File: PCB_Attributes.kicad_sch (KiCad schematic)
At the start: 0 parts

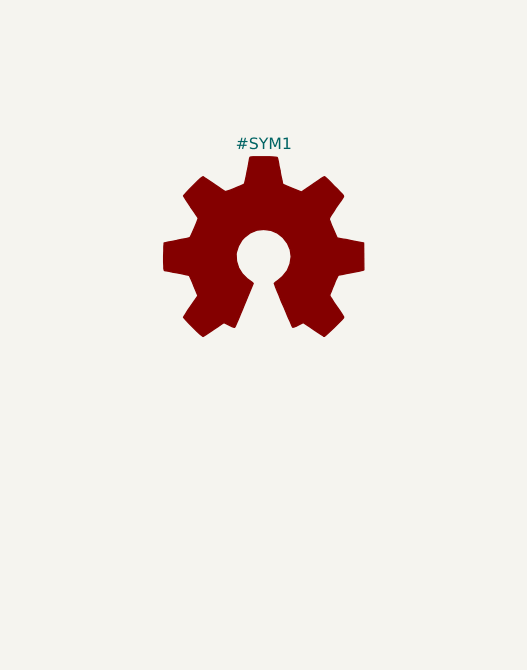
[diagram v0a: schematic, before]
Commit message: Changed GPIO headers to Arduino style
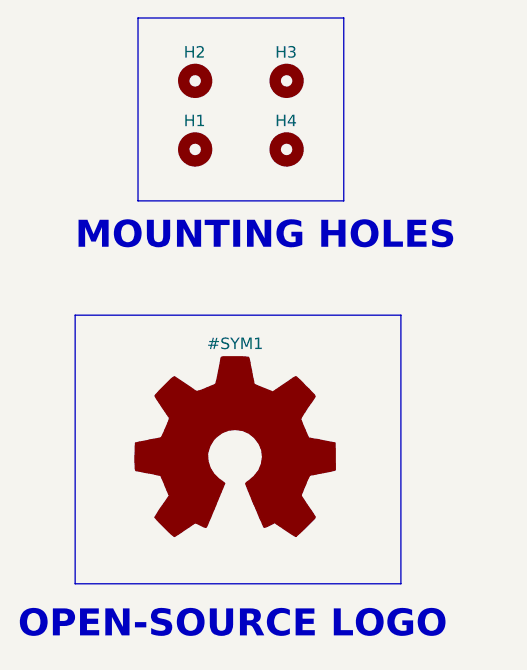
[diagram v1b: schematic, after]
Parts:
- added H1, H2, H3, H4: MountingHole, symbol ESP32-S3_DB:MountingHole
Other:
- note added: "MOUNTING HOLES"
- note added: "OPEN-SOURCE LOGO"
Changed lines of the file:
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@@
 (kicad_sch (version 20230121) (generator eeschema)
   (paper "A4")
-  (symbol (lib_id "ESP32-S3_DB:Logo_Open_Hardware_Large") (at 151.13 99.695 0) (unit 1)
+  (bus (pts (xy 130.175 106.045) (xy 166.37 106.045))
+    (stroke (width 1) (type default) (color 72 72 72 1))
+  )
+  (bus (pts (xy 130.175 135.89) (xy 130.175 106.045))
+    (stroke (width 1) (type default) (color 72 72 72 1))
+  )
+  (bus (pts (xy 166.37 106.045) (xy 166.37 135.89))
+    (stroke (width 1) (type default) (color 72 72 72 1))
+  )
+  (bus (pts (xy 130.175 135.89) (xy 166.37 135.89))
+    (stroke (width 1) (type default) (color 72 72 72 1))
+  )
+  (bus (pts (xy 137.16 93.345) (xy 137.16 73.025))
+    (stroke (width 1) (type default) (color 72 72 72 1))
+  )
+  (bus (pts (xy 137.16 93.345) (xy 160.02 93.345))
+    (stroke (width 1) (type default) (color 72 72 72 1))
+  )
+  (bus (pts (xy 137.16 73.025) (xy 160.02 73.025))
+    (stroke (width 1) (type default) (color 72 72 72 1))
+  )
+  (bus (pts (xy 160.02 73.025) (xy 160.02 93.345))
+    (stroke (width 1) (type default) (color 72 72 72 1))
+  )
+  (text "OPEN-SOURCE LOGO" (at 123.825 142.24 0)
+    (effects (font (size 3 3) bold (color 255 0 0 1)) (justify left bottom))
+  )
+  (text "MOUNTING HOLES" (at 130.175 99.06 0)
+    (effects (font (size 3 3) bold (color 255 0 0 1)) (justify left bottom))
+  )
+  (symbol (lib_id "ESP32-S3_DB:MountingHole") (at 143.51 87.63 0) (unit 1)
+    (in_bom yes) (on_board yes) (dnp no)
+    (property "Reference" "H1" (at 142.24 84.455 0)
+      (effects (font (size 1.27 1.27)) (justify left))
+    )
+    (property "Value" "MountingHole" (at 146.05 88.9 0)
+      (effects (font (size 1.27 1.27)) (justify left) hide)
+    )
+    (property "Footprint" "" (at 143.51 87.63 0)
+      (effects (font (size 1.27 1.27)) hide)
+    )
+    (property "Datasheet" "~" (at 143.51 87.63 0)
+      (effects (font (size 1.27 1.27)) hide)
+    )
+    (instances
+      (project "ESP32-S3_DB"
+        (path "/b7fc4bd3-c219-4455-832b-8d795385dcf1/7ada9602-7e0d-4ea4-a634-9a5d8155ae8b"
+          (reference "H1") (unit 1)
+        )
+      )
+    )
+  )
+  (symbol (lib_id "ESP32-S3_DB:MountingHole") (at 153.67 80.01 0) (unit 1)
+    (in_bom yes) (on_board yes) (dnp no)
+    (property "Reference" "H3" (at 152.4 76.835 0)
+      (effects (font (size 1.27 1.27)) (justify left))
+    )
+    (property "Value" "MountingHole" (at 156.21 81.28 0)
+      (effects (font (size 1.27 1.27)) (justify left) hide)
+    )
+    (property "Footprint" "" (at 153.67 80.01 0)
+      (effects (font (size 1.27 1.27)) hide)
+    )
+    (property "Datasheet" "~" (at 153.67 80.01 0)
+      (effects (font (size 1.27 1.27)) hide)
+    )
+    (instances
+      (project "ESP32-S3_DB"
+        (path "/b7fc4bd3-c219-4455-832b-8d795385dcf1/7ada9602-7e0d-4ea4-a634-9a5d8155ae8b"
+          (reference "H3") (unit 1)
+        )
+      )
+    )
+  )
+  (symbol (lib_id "ESP32-S3_DB:MountingHole") (at 153.67 87.63 0) (unit 1)
+    (in_bom yes) (on_board yes) (dnp no)
+    (property "Reference" "H4" (at 152.4 84.455 0)
+      (effects (font (size 1.27 1.27)) (justify left))
+    )
+    (property "Value" "MountingHole" (at 156.21 88.9 0)
+      (effects (font (size 1.27 1.27)) (justify left) hide)
+    )
+    (property "Footprint" "" (at 153.67 87.63 0)
+      (effects (font (size 1.27 1.27)) hide)
+    )
+    (property "Datasheet" "~" (at 153.67 87.63 0)
+      (effects (font (size 1.27 1.27)) hide)
+    )
+    (instances
+      (project "ESP32-S3_DB"
+        (path "/b7fc4bd3-c219-4455-832b-8d795385dcf1/7ada9602-7e0d-4ea4-a634-9a5d8155ae8b"
+          (reference "H4") (unit 1)
+        )
+      )
+    )
+  )
+  (symbol (lib_id "ESP32-S3_DB:Logo_Open_Hardware_Large") (at 147.955 121.92 0) (unit 1)
     (in_bom no) (on_board no) (dnp no) (fields_autoplaced)
-    (property "Reference" "#SYM1" (at 151.13 86.995 0)
+    (property "Reference" "#SYM1" (at 147.955 109.22 0)
       (effects (font (size 1.27 1.27)))
     )
-    (property "Value" "Logo_Open_Hardware_Large" (at 151.13 109.855 0)
+    (property "Value" "Logo_Open_Hardware_Large" (at 147.955 132.08 0)
       (effects (font (size 1.27 1.27)) hide)
     )
-    (property "Footprint" "ESP32-S3_Dev_Board:OSHW-Symbol_6.7x6mm_SilkScreen" (at 151.13 99.695 0)
+    (property "Footprint" "ESP32-S3_Dev_Board:OSHW-Symbol_6.7x6mm_SilkScreen" (at 147.955 121.92 0)
       (effects (font (size 1.27 1.27)) hide)
     )
-    (property "Datasheet" "~" (at 151.13 99.695 0)
+    (property "Datasheet" "~" (at 147.955 121.92 0)
       (effects (font (size 1.27 1.27)) hide)
     )
-    (property "Sim.Enable" "0" (at 151.13 99.695 0)
+    (property "Sim.Enable" "0" (at 147.955 121.92 0)
       (effects (font (size 1.27 1.27)) hide)
     )
@@
         )
       )
+    )
+  )
+  (symbol (lib_id "ESP32-S3_DB:MountingHole") (at 143.51 80.01 0) (unit 1)
+    (in_bom yes) (on_board yes) (dnp no)
+    (property "Reference" "H2" (at 142.24 76.835 0)
+      (effects (font (size 1.27 1.27)) (justify left))
+    )
+    (property "Value" "MountingHole" (at 146.05 81.28 0)
+      (effects (font (size 1.27 1.27)) (justify left) hide)
+    )
+    (property "Footprint" "" (at 143.51 80.01 0)
+      (effects (font (size 1.27 1.27)) hide)
+    )
+    (property "Datasheet" "~" (at 143.51 80.01 0)
+      (effects (font (size 1.27 1.27)) hide)
+    )
+    (instances
+      (project "ESP32-S3_DB"
+        (path "/b7fc4bd3-c219-4455-832b-8d795385dcf1/7ada9602-7e0d-4ea4-a634-9a5d8155ae8b"
+          (reference "H2") (unit 1)
+        )
+      )

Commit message: First draft of component layout
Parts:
- added SYM1: Logo_Open_Hardware_Large, ESP32-S3_Dev_Board:OSHW-Symbol_6.7x6mm_SilkScreen, symbol ESP32-S3_DB:Logo_Open_Hardware_Large
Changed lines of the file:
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@@
   (symbol (lib_id "ESP32-S3_DB:Logo_Open_Hardware_Large") (at 147.955 121.92 0) (unit 1)
     (in_bom no) (on_board no) (dnp no) (fields_autoplaced)
-    (property "Reference" "#SYM1" (at 147.955 109.22 0)
+    (property "Reference" "SYM1" (at 147.955 109.22 0)
       (effects (font (size 1.27 1.27)))
     )
@@
       (project "ESP32-S3_DB"
         (path "/b7fc4bd3-c219-4455-832b-8d795385dcf1/7ada9602-7e0d-4ea4-a634-9a5d8155ae8b"
-          (reference "#SYM1") (unit 1)
+          (reference "SYM1") (unit 1)
         )
       )

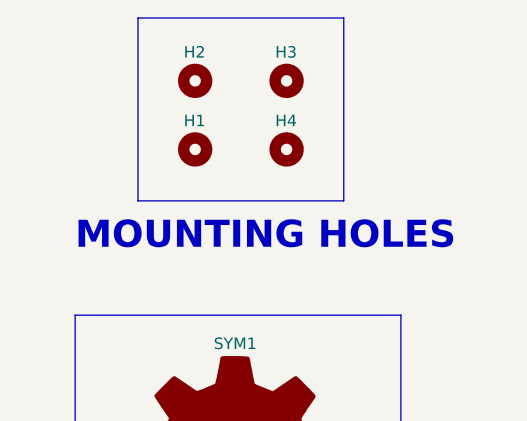
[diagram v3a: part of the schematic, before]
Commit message: Added mounting holes
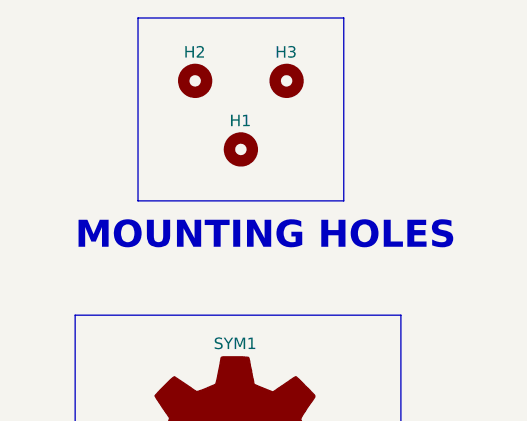
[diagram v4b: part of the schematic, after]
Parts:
- removed H4: MountingHole, symbol ESP32-S3_DB:MountingHole
- H1, H2, H3: footprint (none) -> ESP32-S3_Dev_Board:MountingHole_3.2mm_M3
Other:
- moved on the sheet: H1
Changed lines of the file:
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@@
     (effects (font (size 3 3) bold (color 255 0 0 1)) (justify left bottom))
   )
-  (symbol (lib_id "ESP32-S3_DB:MountingHole") (at 143.51 87.63 0) (unit 1)
+  (symbol (lib_id "ESP32-S3_DB:MountingHole") (at 148.59 87.63 0) (unit 1)
     (in_bom yes) (on_board yes) (dnp no)
-    (property "Reference" "H1" (at 142.24 84.455 0)
+    (property "Reference" "H1" (at 147.32 84.455 0)
       (effects (font (size 1.27 1.27)) (justify left))
     )
-    (property "Value" "MountingHole" (at 146.05 88.9 0)
+    (property "Value" "MountingHole" (at 151.13 88.9 0)
       (effects (font (size 1.27 1.27)) (justify left) hide)
     )
-    (property "Footprint" "" (at 143.51 87.63 0)
+    (property "Footprint" "ESP32-S3_Dev_Board:MountingHole_3.2mm_M3" (at 148.59 87.63 0)
       (effects (font (size 1.27 1.27)) hide)
     )
-    (property "Datasheet" "~" (at 143.51 87.63 0)
+    (property "Datasheet" "~" (at 148.59 87.63 0)
       (effects (font (size 1.27 1.27)) hide)
     )
@@
       (effects (font (size 1.27 1.27)) (justify left) hide)
     )
-    (property "Footprint" "" (at 153.67 80.01 0)
+    (property "Footprint" "ESP32-S3_Dev_Board:MountingHole_3.2mm_M3" (at 153.67 80.01 0)
       (effects (font (size 1.27 1.27)) hide)
     )
@@
     )
   )
-  (symbol (lib_id "ESP32-S3_DB:MountingHole") (at 153.67 87.63 0) (unit 1)
-    (in_bom yes) (on_board yes) (dnp no)
-    (property "Reference" "H4" (at 152.4 84.455 0)
-      (effects (font (size 1.27 1.27)) (justify left))
-    )
-    (property "Value" "MountingHole" (at 156.21 88.9 0)
-      (effects (font (size 1.27 1.27)) (justify left) hide)
-    )
-    (property "Footprint" "" (at 153.67 87.63 0)
-      (effects (font (size 1.27 1.27)) hide)
-    )
-    (property "Datasheet" "~" (at 153.67 87.63 0)
-      (effects (font (size 1.27 1.27)) hide)
-    )
-    (instances
-      (project "ESP32-S3_DB"
-        (path "/b7fc4bd3-c219-4455-832b-8d795385dcf1/7ada9602-7e0d-4ea4-a634-9a5d8155ae8b"
-          (reference "H4") (unit 1)
-        )
-        (path "/b7fc4bd3-c219-4455-832b-8d795385dcf1/f98b3539-fa8a-48eb-9a00-f8d7da317cf1"
-          (reference "H8") (unit 1)
-        )
-      )
-    )
-  )
   (symbol (lib_id "ESP32-S3_DB:Logo_Open_Hardware_Large") (at 147.955 121.92 0) (unit 1)
     (in_bom no) (on_board no) (dnp no) (fields_autoplaced)
@@
     )
     (property "Datasheet" "~" (at 147.955 121.92 0)
-      (effects (font (size 1.27 1.27)) hide)
-    )
-    (property "Sim.Enable" "0" (at 147.955 121.92 0)
       (effects (font (size 1.27 1.27)) hide)
     )
@@
       (effects (font (size 1.27 1.27)) (justify left) hide)
     )
-    (property "Footprint" "" (at 143.51 80.01 0)
+    (property "Footprint" "ESP32-S3_Dev_Board:MountingHole_3.2mm_M3" (at 143.51 80.01 0)
       (effects (font (size 1.27 1.27)) hide)
     )

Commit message: Finished routing
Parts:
- added SYM2: Logo_Open_Hardware_Large, ESP32-S3_Dev_Board:OSHW-Symbol_6.7x6mm_Copper, symbol ESP32-S3_DB:Logo_Open_Hardware_Large
- SYM1: footprint ESP32-S3_Dev_Board:OSHW-Symbol_6.7x6mm_SilkScreen -> ESP32-S3_Dev_Board:OSHW-Symbol_6.7x6mm_Copper
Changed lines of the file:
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@@
 (kicad_sch (version 20230121) (generator eeschema)
   (paper "A4")
-  (bus (pts (xy 130.175 106.045) (xy 166.37 106.045))
+  (bus (pts (xy 130.175 106.045) (xy 203.835 106.045))
     (stroke (width 1) (type default) (color 72 72 72 1))
   )
@@
     (stroke (width 1) (type default) (color 72 72 72 1))
   )
-  (bus (pts (xy 166.37 106.045) (xy 166.37 135.89))
+  (bus (pts (xy 203.835 106.045) (xy 203.835 135.89))
     (stroke (width 1) (type default) (color 72 72 72 1))
   )
-  (bus (pts (xy 130.175 135.89) (xy 166.37 135.89))
+  (bus (pts (xy 130.175 135.89) (xy 203.835 135.89))
     (stroke (width 1) (type default) (color 72 72 72 1))
   )
@@
     (stroke (width 1) (type default) (color 72 72 72 1))
   )
-  (text "OPEN-SOURCE LOGO" (at 123.825 142.24 0)
+  (text "OPEN-SOURCE LOGO" (at 143.51 142.875 0)
     (effects (font (size 3 3) bold (color 255 0 0 1)) (justify left bottom))
   )
@@
     )
   )
+  (symbol (lib_id "ESP32-S3_DB:Logo_Open_Hardware_Large") (at 187.96 121.92 0) (unit 1)
+    (in_bom no) (on_board no) (dnp no) (fields_autoplaced)
+    (property "Reference" "SYM2" (at 187.96 109.22 0)
+      (effects (font (size 1.27 1.27)))
+    )
+    (property "Value" "Logo_Open_Hardware_Large" (at 187.96 132.08 0)
+      (effects (font (size 1.27 1.27)) hide)
+    )
+    (property "Footprint" "ESP32-S3_Dev_Board:OSHW-Symbol_6.7x6mm_Copper" (at 187.96 121.92 0)
+      (effects (font (size 1.27 1.27)) hide)
+    )
+    (property "Datasheet" "~" (at 187.96 121.92 0)
+      (effects (font (size 1.27 1.27)) hide)
+    )
+    (instances
+      (project "ESP32-S3_DB"
+        (path "/b7fc4bd3-c219-4455-832b-8d795385dcf1/7ada9602-7e0d-4ea4-a634-9a5d8155ae8b"
+          (reference "SYM2") (unit 1)
+        )
+        (path "/b7fc4bd3-c219-4455-832b-8d795385dcf1/f98b3539-fa8a-48eb-9a00-f8d7da317cf1"
+          (reference "SYM2") (unit 1)
+        )
+      )
+    )
+  )
   (symbol (lib_id "ESP32-S3_DB:Logo_Open_Hardware_Large") (at 147.955 121.92 0) (unit 1)
     (in_bom no) (on_board no) (dnp no) (fields_autoplaced)
@@
       (effects (font (size 1.27 1.27)) hide)
     )
-    (property "Footprint" "ESP32-S3_Dev_Board:OSHW-Symbol_6.7x6mm_SilkScreen" (at 147.955 121.92 0)
+    (property "Footprint" "ESP32-S3_Dev_Board:OSHW-Symbol_6.7x6mm_Copper" (at 147.955 121.92 0)
       (effects (font (size 1.27 1.27)) hide)
     )
